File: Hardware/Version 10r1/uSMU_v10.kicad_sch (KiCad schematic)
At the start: 131 parts, among them J1 SWD, J2 USB_C_Receptacle_USB2.0, J3 DUT, Q1 AO3401A, U1 ADS1115IDGS, U10 LT1970, U11 DAC8571IDGKR, U12 TPS65131RGET, U13 H7650-45PR, U14 PGA281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

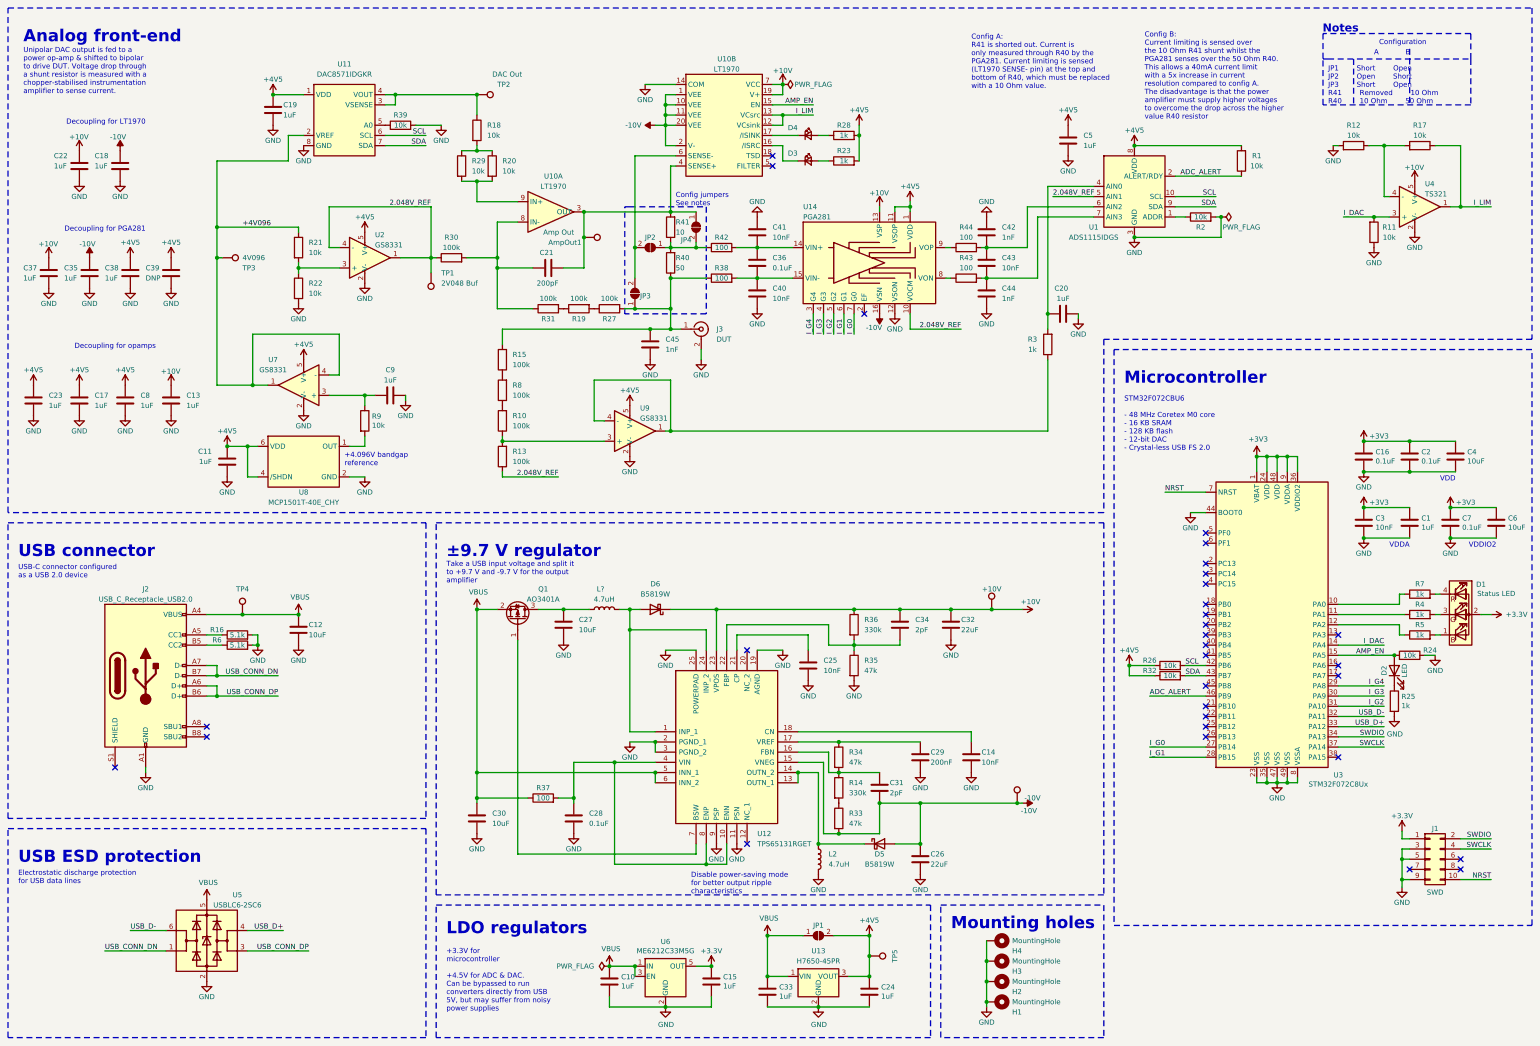
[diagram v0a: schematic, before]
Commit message: Hardware: back-annotate schematics from PCB
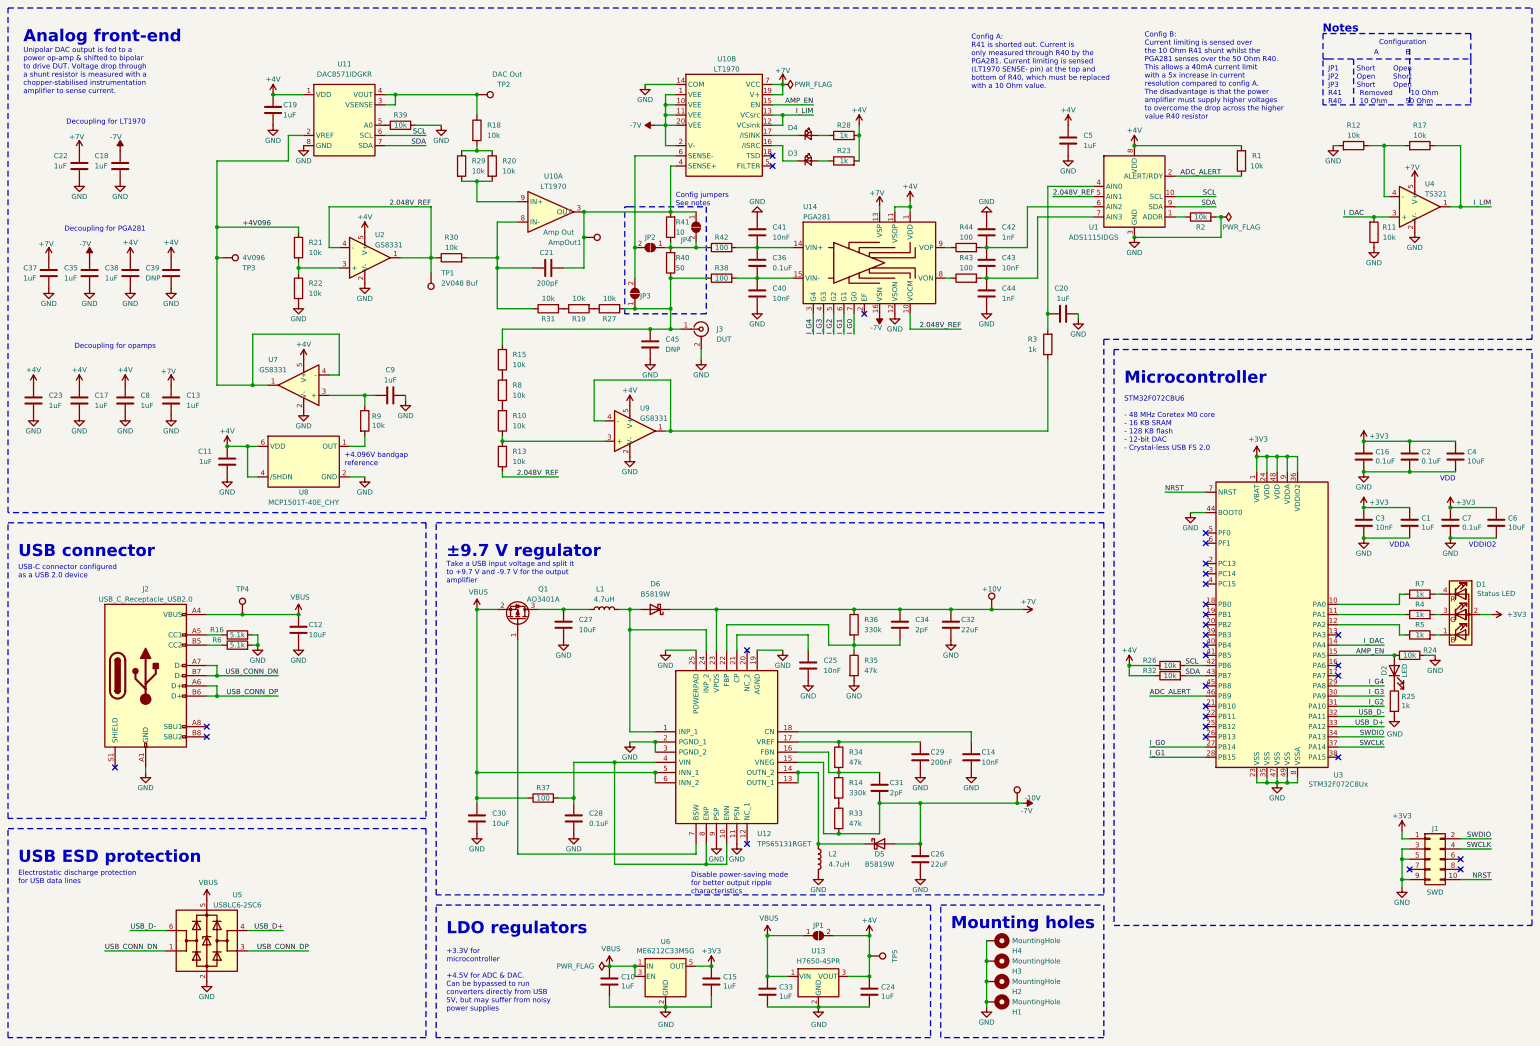
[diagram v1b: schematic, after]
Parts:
- C45: value 1nF -> DNP
- D1: footprint uSMU_v10:E6C0606RGBC3UDA -> uSMU-simple_v1:E6C0606RGBC3UDA
- L1: renamed from L?; LCSC# (none) -> C5832388
- R10, R13, R15, R19, R27, R30, R31, R8: value 100k -> 10k
- U12: footprint QFN50P400X400X100-25N -> Package_DFN_QFN:VQFN-24-1EP_4x4mm_P0.5mm_EP2.45x2.45mm_ThermalVias
